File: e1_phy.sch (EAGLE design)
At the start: 125 parts, among them IC2 LD117AS33TR, IC3 LD117AS33TR, IC4 MCP4725, U1 IDT82V2081, U2 GPS_GNS_2201, U3 VCTCXO-CONNORWINFIELD, U4 VCXO_TAITIEN_VT, U5 IP4234CZ6, X2 SMA-142-0701-801/806, X3 JACK2.5_SJ-2523, X4 0446200002

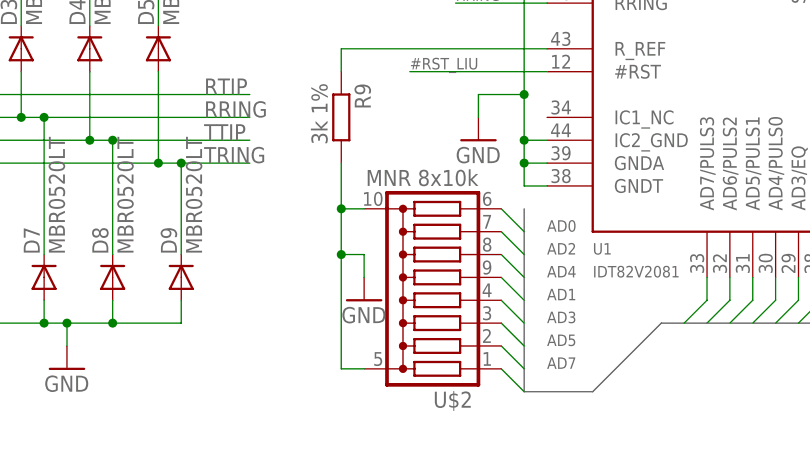
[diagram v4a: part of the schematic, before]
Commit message: Implementation of review comment:
   Removed octal resistor array, introduced quad resistor array,
   will be used for various pullups.
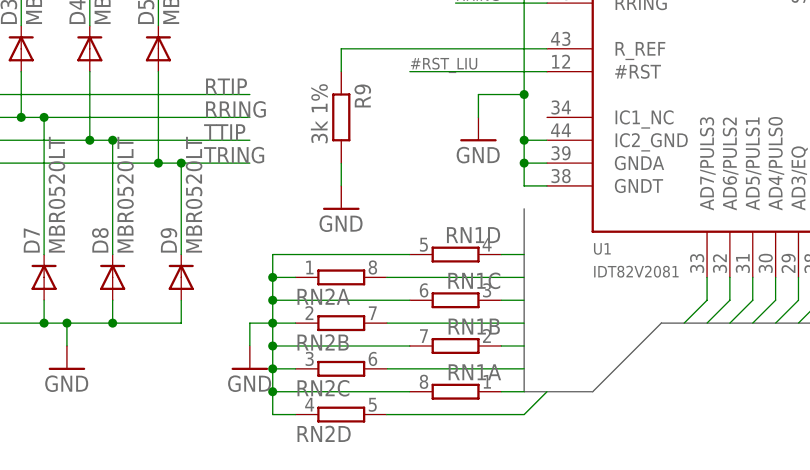
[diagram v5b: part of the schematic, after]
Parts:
- removed U$2: MNR 8x10k, laforge:MNR
- added RN1, RN2: (no value), resistor-dil:4R-NEXB38V
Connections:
- net AD0: now also RN2A.2; no longer U$2.8
- net AD1: now also RN2B.2; no longer U$2.4
- net AD2: now also RN2C.2; no longer U$2.7
- net AD3: now also RN2D.2; no longer U$2.3
- net AD4: now also RN1D.1; no longer U$2.6
- net AD5: now also RN1C.1; no longer U$2.2
- net AD6: now also RN1B.1; no longer U$2.5
- net AD7: now also RN1A.1; no longer U$2.1
- net GND: now also RN1A.2, RN1B.2, RN1C.2, RN1D.2, RN2A.1, RN2B.1, RN2C.1, RN2D.1; no longer U$2.C, U$2.D
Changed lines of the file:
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@@
 <part name="GND7" library="supply1" deviceset="GND" device=""/>
 <part name="GND8" library="supply1" deviceset="GND" device=""/>
-<part name="U$2" library="laforge" deviceset="MNR" device="" value="MNR 8x10k"/>
 <part name="GND9" library="supply1" deviceset="GND" device=""/>
 <part name="TR1" library="laforge" deviceset="PULSE_T1094NL" device=""/>
@@
 <part name="U5" library="laforge" deviceset="IP4234CZ6" device=""/>
 <part name="GND12" library="supply1" deviceset="GND" device=""/>
+<part name="RN1" library="resistor-dil" library_urn="urn:adsk.eagle:library:342" deviceset="4R-N" device="EXB38V" package3d_urn="urn:adsk.eagle:package:24923/1"/>
+<part name="RN2" library="resistor-dil" library_urn="urn:adsk.eagle:library:342" deviceset="4R-N" device="EXB38V" package3d_urn="urn:adsk.eagle:package:24923/1"/>
+<part name="GND28" library="supply1" deviceset="GND" device=""/>
 </parts>
 <sheets>
@@
 </instance>
 <instance part="GND8" gate="1" x="238.76" y="10.16"/>
-<instance part="U$2" gate="G$1" x="185.42" y="17.78" rot="R180"/>
-<instance part="GND9" gate="1" x="177.8" y="15.24"/>
+<instance part="GND9" gate="1" x="175.26" y="25.4"/>
 <instance part="TR1" gate="-1:1" x="93.98" y="40.64" rot="MR0"/>
 <instance part="TR1" gate="-1:2" x="93.98" y="17.78" rot="MR0"/>
@@
 <instance part="U5" gate="G$1" x="43.18" y="243.84"/>
 <instance part="GND12" gate="1" x="43.18" y="228.6"/>
+<instance part="RN1" gate="A" x="187.96" y="5.08" rot="R180"/>
+<instance part="RN1" gate="B" x="187.96" y="10.16" rot="R180"/>
+<instance part="RN1" gate="C" x="187.96" y="15.24" rot="R180"/>
+<instance part="RN1" gate="D" x="187.96" y="20.32" rot="R180"/>
+<instance part="RN2" gate="A" x="175.26" y="17.78"/>
+<instance part="RN2" gate="B" x="175.26" y="12.7"/>
+<instance part="RN2" gate="C" x="175.26" y="7.62"/>
+<instance part="RN2" gate="D" x="175.26" y="2.54"/>
+<instance part="GND28" gate="1" x="165.1" y="7.62"/>
 </instances>
 <busses>
@@
 </segment>
 <segment>
-<pinref part="U$2" gate="G$1" pin="C"/>
-<wire x1="177.8" y1="7.62" x2="175.26" y2="7.62" width="0.1524" layer="91"/>
 <pinref part="GND9" gate="1" pin="GND"/>
-<wire x1="175.26" y1="7.62" x2="175.26" y2="20.32" width="0.1524" layer="91"/>
-<pinref part="U$2" gate="G$1" pin="D"/>
-<wire x1="175.26" y1="20.32" x2="175.26" y2="25.4" width="0.1524" layer="91"/>
-<wire x1="175.26" y1="25.4" x2="177.8" y2="25.4" width="0.1524" layer="91"/>
-<wire x1="177.8" y1="17.78" x2="177.8" y2="20.32" width="0.1524" layer="91"/>
-<wire x1="177.8" y1="20.32" x2="175.26" y2="20.32" width="0.1524" layer="91"/>
-<junction x="175.26" y="20.32"/>
 <pinref part="R9" gate="G$1" pin="2"/>
-<wire x1="175.26" y1="30.48" x2="175.26" y2="25.4" width="0.1524" layer="91"/>
-<junction x="175.26" y="25.4"/>
+<wire x1="175.26" y1="30.48" x2="175.26" y2="27.94" width="0.1524" layer="91"/>
 </segment>
 <segment>
@@
 <pinref part="GND12" gate="1" pin="GND"/>
 <wire x1="43.18" y1="233.68" x2="43.18" y2="231.14" width="0.1524" layer="91"/>
+</segment>
+<segment>
+<pinref part="GND28" gate="1" pin="GND"/>
+<wire x1="165.1" y1="10.16" x2="165.1" y2="12.7" width="0.1524" layer="91"/>
+<pinref part="RN1" gate="D" pin="2"/>
+<wire x1="182.88" y1="20.32" x2="167.64" y2="20.32" width="0.1524" layer="91"/>
+<pinref part="RN2" gate="A" pin="1"/>
+<wire x1="170.18" y1="17.78" x2="167.64" y2="17.78" width="0.1524" layer="91"/>
+<wire x1="167.64" y1="17.78" x2="167.64" y2="20.32" width="0.1524" layer="91"/>
+<pinref part="RN1" gate="C" pin="2"/>
+<wire x1="182.88" y1="15.24" x2="167.64" y2="15.24" width="0.1524" layer="91"/>
+<wire x1="167.64" y1="15.24" x2="167.64" y2="17.78" width="0.1524" layer="91"/>
+<junction x="167.64" y="17.78"/>
+<pinref part="RN1" gate="B" pin="2"/>
+<wire x1="182.88" y1="10.16" x2="167.64" y2="10.16" width="0.1524" layer="91"/>
+<wire x1="167.64" y1="10.16" x2="167.64" y2="12.7" width="0.1524" layer="91"/>
+<junction x="167.64" y="15.24"/>
+<pinref part="RN2" gate="B" pin="1"/>
+<wire x1="167.64" y1="12.7" x2="167.64" y2="15.24" width="0.1524" layer="91"/>
+<wire x1="170.18" y1="12.7" x2="167.64" y2="12.7" width="0.1524" layer="91"/>
+<junction x="167.64" y="12.7"/>
+<pinref part="RN2" gate="C" pin="1"/>
+<wire x1="170.18" y1="7.62" x2="167.64" y2="7.62" width="0.1524" layer="91"/>
+<wire x1="167.64" y1="7.62" x2="167.64" y2="10.16" width="0.1524" layer="91"/>
+<junction x="167.64" y="10.16"/>
+<pinref part="RN2" gate="D" pin="1"/>
+<wire x1="170.18" y1="2.54" x2="167.64" y2="2.54" width="0.1524" layer="91"/>
+<wire x1="167.64" y1="2.54" x2="167.64" y2="5.08" width="0.1524" layer="91"/>
+<junction x="167.64" y="7.62"/>
+<pinref part="RN1" gate="A" pin="2"/>
+<wire x1="167.64" y1="5.08" x2="167.64" y2="7.62" width="0.1524" layer="91"/>
+<wire x1="182.88" y1="5.08" x2="167.64" y2="5.08" width="0.1524" layer="91"/>
+<junction x="167.64" y="5.08"/>
+<wire x1="165.1" y1="12.7" x2="167.64" y2="12.7" width="0.1524" layer="91"/>
 </segment>
 </net>
@@
 </segment>
 <segment>
-<pinref part="U$2" gate="G$1" pin="8"/>
-<wire x1="193.04" y1="25.4" x2="195.58" y2="22.86" width="0.1524" layer="91"/>
-<label x="198.12" y="22.86" size="1.27" layer="95"/>
+<pinref part="RN2" gate="A" pin="2"/>
+<wire x1="195.58" y1="17.78" x2="180.34" y2="17.78" width="0.1524" layer="91"/>
 </segment>
 </net>
@@
 </segment>
 <segment>
-<pinref part="U$2" gate="G$1" pin="4"/>
-<wire x1="193.04" y1="15.24" x2="195.58" y2="12.7" width="0.1524" layer="91"/>
-<label x="198.12" y="15.24" size="1.27" layer="95"/>
+<pinref part="RN2" gate="B" pin="2"/>
+<wire x1="195.58" y1="12.7" x2="180.34" y2="12.7" width="0.1524" layer="91"/>
 </segment>
 </net>
@@
 </segment>
 <segment>
-<pinref part="U$2" gate="G$1" pin="7"/>
-<wire x1="193.04" y1="22.86" x2="195.58" y2="20.32" width="0.1524" layer="91"/>
-<label x="198.12" y="20.32" size="1.27" layer="95"/>
+<pinref part="RN2" gate="C" pin="2"/>
+<wire x1="195.58" y1="7.62" x2="180.34" y2="7.62" width="0.1524" layer="91"/>
 </segment>
 </net>
@@
 </segment>
 <segment>
-<pinref part="U$2" gate="G$1" pin="3"/>
-<wire x1="193.04" y1="12.7" x2="195.58" y2="10.16" width="0.1524" layer="91"/>
-<label x="198.12" y="12.7" size="1.27" layer="95"/>
+<pinref part="RN2" gate="D" pin="2"/>
+<wire x1="180.34" y1="2.54" x2="195.58" y2="2.54" width="0.1524" layer="91"/>
+<wire x1="198.12" y1="5.08" x2="195.58" y2="2.54" width="0.1524" layer="91"/>
 </segment>
 </net>
@@
 </segment>
 <segment>
-<pinref part="U$2" gate="G$1" pin="6"/>
-<wire x1="193.04" y1="20.32" x2="195.58" y2="17.78" width="0.1524" layer="91"/>
-<label x="198.12" y="17.78" size="1.27" layer="95"/>
+<pinref part="RN1" gate="D" pin="1"/>
+<wire x1="193.04" y1="20.32" x2="195.58" y2="20.32" width="0.1524" layer="91"/>
 </segment>
 </net>
@@
 </segment>
 <segment>
-<pinref part="U$2" gate="G$1" pin="2"/>
-<wire x1="193.04" y1="10.16" x2="195.58" y2="7.62" width="0.1524" layer="91"/>
-<label x="198.12" y="10.16" size="1.27" layer="95"/>
+<pinref part="RN1" gate="C" pin="1"/>
+<wire x1="193.04" y1="15.24" x2="195.58" y2="15.24" width="0.1524" layer="91"/>
 </segment>
 </net>
@@
 </segment>
 <segment>
-<pinref part="U$2" gate="G$1" pin="5"/>
-<wire x1="193.04" y1="17.78" x2="195.58" y2="15.24" width="0.1524" layer="91"/>
+<pinref part="RN1" gate="B" pin="1"/>
+<wire x1="193.04" y1="10.16" x2="195.58" y2="10.16" width="0.1524" layer="91"/>
 </segment>
 </net>
@@
 </segment>
 <segment>
-<pinref part="U$2" gate="G$1" pin="1"/>
-<wire x1="193.04" y1="7.62" x2="195.58" y2="5.08" width="0.1524" layer="91"/>
-<label x="198.12" y="7.62" size="1.27" layer="95"/>
-</segment>
-</net>
+<pinref part="RN1" gate="A" pin="1"/>
+<wire x1="193.04" y1="5.08" x2="195.58" y2="5.08" width="0.1524" layer="91"/>
+</segment>
+</net>

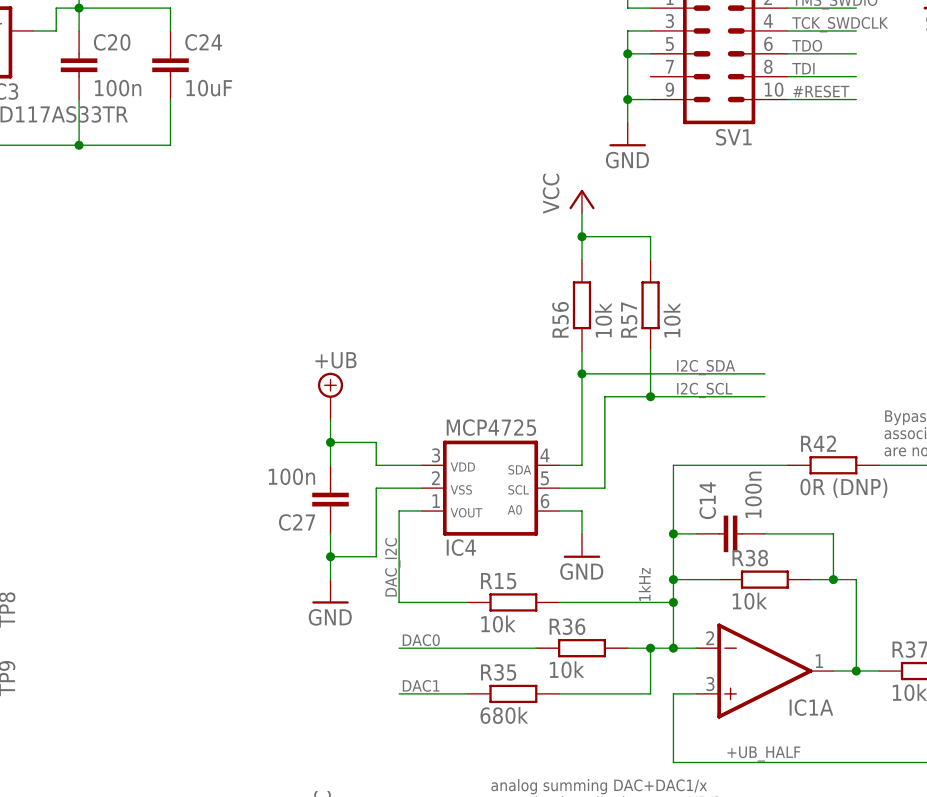
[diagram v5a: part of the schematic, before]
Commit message: Implement review comments: Switch DAC to Maxim part.
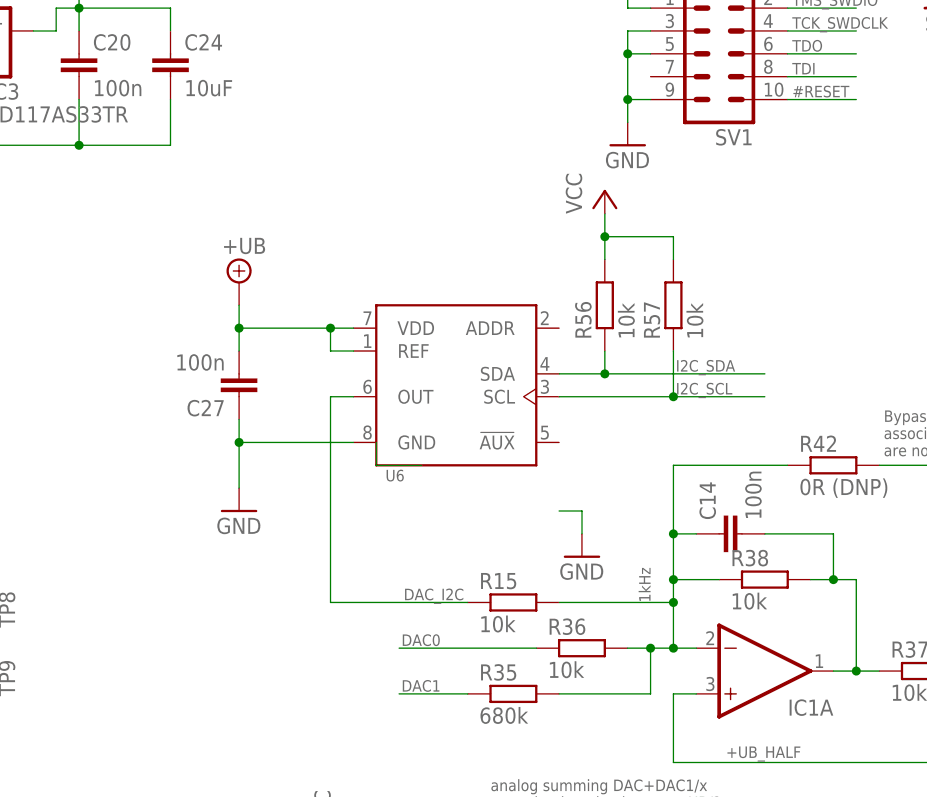
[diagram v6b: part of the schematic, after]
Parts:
- removed IC4: MCP4725, dp_devices:IC_MCP4725
- added U6: (no value), max5215_max5217:MAX521X
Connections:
- net +UB: now also U6.REF, U6.VDD; no longer IC4.3
- net DAC_I2C: now also U6.OUT; no longer IC4.1
- net GND: now also U6.GND; no longer IC4.2, IC4.6
- net I2C_SCL: now also U6.SCL; no longer IC4.5
- net I2C_SDA: now also U6.SDA; no longer IC4.4
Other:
- moved on the sheet: C27, R56, R57
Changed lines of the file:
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@@
 <part name="TP14" library="testpad" deviceset="TP" device="B1,27"/>
 <part name="TP15" library="testpad" deviceset="TP" device="B1,27"/>
-<part name="IC4" library="dp_devices" deviceset="IC_MCP4725" device="" value="MCP4725"/>
 <part name="C27" library="rcl" deviceset="C-EU" device="C0603" value="100n"/>
 <part name="SUPPLY7" library="supply2" deviceset="+UB" device=""/>
@@
 <part name="RN2" library="resistor-dil" library_urn="urn:adsk.eagle:library:342" deviceset="4R-N" device="EXB38V" package3d_urn="urn:adsk.eagle:package:24923/1"/>
 <part name="GND28" library="supply1" deviceset="GND" device=""/>
+<part name="U6" library="max5215_max5217" deviceset="MAX521X" device=""/>
 </parts>
 <sheets>
@@
 <instance part="TP14" gate="G$1" x="109.22" y="106.68" rot="R180"/>
 <instance part="TP15" gate="G$1" x="111.76" y="104.14" rot="R180"/>
-<instance part="IC4" gate="G$1" x="233.68" y="195.58" rot="MR180"/>
-<instance part="C27" gate="G$1" x="215.9" y="193.04" rot="R180"/>
-<instance part="SUPPLY7" gate="G$1" x="215.9" y="205.74"/>
-<instance part="GND34" gate="1" x="215.9" y="182.88"/>
+<instance part="C27" gate="G$1" x="205.74" y="205.74" rot="R180"/>
+<instance part="SUPPLY7" gate="G$1" x="205.74" y="218.44"/>
+<instance part="GND34" gate="1" x="205.74" y="193.04"/>
 <instance part="R15" gate="G$1" x="236.22" y="182.88"/>
 <instance part="GND35" gate="1" x="243.84" y="187.96"/>
@@
 </instance>
 <instance part="GND30" gate="G$1" x="20.32" y="48.26"/>
-<instance part="R56" gate="G$1" x="243.84" y="215.9" rot="R90"/>
-<instance part="R57" gate="G$1" x="251.46" y="215.9" rot="R90"/>
-<instance part="P+4" gate="VCC" x="243.84" y="228.6"/>
+<instance part="R56" gate="G$1" x="246.38" y="215.9" rot="R90"/>
+<instance part="R57" gate="G$1" x="254" y="215.9" rot="R90"/>
+<instance part="P+4" gate="VCC" x="246.38" y="228.6"/>
 <instance part="JP2" gate="A" x="144.78" y="210.82" rot="R270"/>
 <instance part="U1" gate="G$1" x="226.06" y="45.72"/>
@@
 <instance part="RN2" gate="D" x="175.26" y="2.54"/>
 <instance part="GND28" gate="1" x="165.1" y="7.62"/>
+<instance part="U6" gate="G$1" x="228.6" y="205.74"/>
 </instances>
 <busses>
@@
 </segment>
 <segment>
+<pinref part="GND34" gate="1" pin="GND"/>
 <pinref part="C27" gate="G$1" pin="1"/>
-<pinref part="GND34" gate="1" pin="GND"/>
-<wire x1="215.9" y1="190.5" x2="215.9" y2="187.96" width="0.1524" layer="91"/>
-<pinref part="IC4" gate="G$1" pin="2"/>
-<wire x1="215.9" y1="187.96" x2="215.9" y2="185.42" width="0.1524" layer="91"/>
-<wire x1="226.06" y1="195.58" x2="220.98" y2="195.58" width="0.1524" layer="91"/>
-<wire x1="220.98" y1="195.58" x2="220.98" y2="187.96" width="0.1524" layer="91"/>
-<wire x1="220.98" y1="187.96" x2="215.9" y2="187.96" width="0.1524" layer="91"/>
-<junction x="215.9" y="187.96"/>
-</segment>
-<segment>
-<pinref part="IC4" gate="G$1" pin="6"/>
+<wire x1="205.74" y1="203.2" x2="205.74" y2="200.66" width="0.1524" layer="91"/>
+<pinref part="U6" gate="G$1" pin="GND"/>
+<wire x1="205.74" y1="200.66" x2="205.74" y2="195.58" width="0.1524" layer="91"/>
+<wire x1="218.44" y1="200.66" x2="205.74" y2="200.66" width="0.1524" layer="91"/>
+<junction x="205.74" y="200.66"/>
+</segment>
+<segment>
 <wire x1="241.3" y1="193.04" x2="243.84" y2="193.04" width="0.1524" layer="91"/>
 <wire x1="243.84" y1="193.04" x2="243.84" y2="190.5" width="0.1524" layer="91"/>
@@
 <pinref part="P+4" gate="VCC" pin="VCC"/>
 <pinref part="R56" gate="G$1" pin="2"/>
-<wire x1="243.84" y1="226.06" x2="243.84" y2="223.52" width="0.1524" layer="91"/>
-<wire x1="243.84" y1="223.52" x2="243.84" y2="220.98" width="0.1524" layer="91"/>
-<wire x1="243.84" y1="223.52" x2="251.46" y2="223.52" width="0.1524" layer="91"/>
-<junction x="243.84" y="223.52"/>
+<wire x1="246.38" y1="226.06" x2="246.38" y2="223.52" width="0.1524" layer="91"/>
+<wire x1="246.38" y1="223.52" x2="246.38" y2="220.98" width="0.1524" layer="91"/>
+<wire x1="246.38" y1="223.52" x2="254" y2="223.52" width="0.1524" layer="91"/>
+<junction x="246.38" y="223.52"/>
 <pinref part="R57" gate="G$1" pin="2"/>
-<wire x1="251.46" y1="223.52" x2="251.46" y2="220.98" width="0.1524" layer="91"/>
+<wire x1="254" y1="223.52" x2="254" y2="220.98" width="0.1524" layer="91"/>
 </segment>
 <segment>
@@
 </segment>
 <segment>
+<pinref part="C27" gate="G$1" pin="2"/>
 <pinref part="SUPPLY7" gate="G$1" pin="+UB"/>
-<pinref part="C27" gate="G$1" pin="2"/>
-<wire x1="215.9" y1="203.2" x2="215.9" y2="200.66" width="0.1524" layer="91"/>
-<pinref part="IC4" gate="G$1" pin="3"/>
-<wire x1="215.9" y1="200.66" x2="215.9" y2="198.12" width="0.1524" layer="91"/>
-<wire x1="226.06" y1="198.12" x2="220.98" y2="198.12" width="0.1524" layer="91"/>
-<wire x1="220.98" y1="198.12" x2="220.98" y2="200.66" width="0.1524" layer="91"/>
-<wire x1="220.98" y1="200.66" x2="215.9" y2="200.66" width="0.1524" layer="91"/>
-<junction x="215.9" y="200.66"/>
+<wire x1="205.74" y1="215.9" x2="205.74" y2="213.36" width="0.1524" layer="91"/>
+<pinref part="U6" gate="G$1" pin="VDD"/>
+<wire x1="205.74" y1="213.36" x2="205.74" y2="210.82" width="0.1524" layer="91"/>
+<wire x1="218.44" y1="213.36" x2="215.9" y2="213.36" width="0.1524" layer="91"/>
+<junction x="205.74" y="213.36"/>
+<pinref part="U6" gate="G$1" pin="REF"/>
+<wire x1="215.9" y1="213.36" x2="205.74" y2="213.36" width="0.1524" layer="91"/>
+<wire x1="218.44" y1="210.82" x2="215.9" y2="210.82" width="0.1524" layer="91"/>
+<wire x1="215.9" y1="210.82" x2="215.9" y2="213.36" width="0.1524" layer="91"/>
+<junction x="215.9" y="213.36"/>
 </segment>
 <segment>
@@
 </segment>
 <segment>
-<pinref part="IC4" gate="G$1" pin="4"/>
-<wire x1="241.3" y1="198.12" x2="243.84" y2="198.12" width="0.1524" layer="91"/>
-<wire x1="243.84" y1="198.12" x2="243.84" y2="208.28" width="0.1524" layer="91"/>
+<wire x1="241.3" y1="208.28" x2="246.38" y2="208.28" width="0.1524" layer="91"/>
 <label x="254.254" y="208.534" size="1.27" layer="95"/>
-<wire x1="243.84" y1="208.28" x2="264.16" y2="208.28" width="0.1524" layer="91"/>
+<wire x1="246.38" y1="208.28" x2="264.16" y2="208.28" width="0.1524" layer="91"/>
 <pinref part="R56" gate="G$1" pin="1"/>
-<wire x1="243.84" y1="210.82" x2="243.84" y2="208.28" width="0.1524" layer="91"/>
-<junction x="243.84" y="208.28"/>
+<wire x1="246.38" y1="210.82" x2="246.38" y2="208.28" width="0.1524" layer="91"/>
+<junction x="246.38" y="208.28"/>
+<pinref part="U6" gate="G$1" pin="SDA"/>
 </segment>
 </net>
@@
 </segment>
 <segment>
-<pinref part="IC4" gate="G$1" pin="5"/>
-<wire x1="241.3" y1="195.58" x2="246.38" y2="195.58" width="0.1524" layer="91"/>
-<wire x1="246.38" y1="195.58" x2="246.38" y2="205.74" width="0.1524" layer="91"/>
 <label x="254.254" y="205.994" size="1.27" layer="95"/>
-<wire x1="246.38" y1="205.74" x2="251.46" y2="205.74" width="0.1524" layer="91"/>
+<wire x1="241.3" y1="205.74" x2="254" y2="205.74" width="0.1524" layer="91"/>
 <pinref part="R57" gate="G$1" pin="1"/>
-<wire x1="251.46" y1="205.74" x2="264.16" y2="205.74" width="0.1524" layer="91"/>
-<wire x1="251.46" y1="210.82" x2="251.46" y2="205.74" width="0.1524" layer="91"/>
-<junction x="251.46" y="205.74"/>
+<wire x1="254" y1="205.74" x2="264.16" y2="205.74" width="0.1524" layer="91"/>
+<wire x1="254" y1="210.82" x2="254" y2="205.74" width="0.1524" layer="91"/>
+<junction x="254" y="205.74"/>
+<pinref part="U6" gate="G$1" pin="SCL"/>
 </segment>
 </net>
@@
 <segment>
 <pinref part="R15" gate="G$1" pin="1"/>
-<wire x1="231.14" y1="182.88" x2="223.52" y2="182.88" width="0.1524" layer="91"/>
-<wire x1="223.52" y1="182.88" x2="223.52" y2="193.04" width="0.1524" layer="91"/>
-<pinref part="IC4" gate="G$1" pin="1"/>
-<wire x1="223.52" y1="193.04" x2="226.06" y2="193.04" width="0.1524" layer="91"/>
-<label x="223.266" y="183.388" size="1.27" layer="95" rot="R90"/>
+<label x="224.028" y="183.134" size="1.27" layer="95"/>
+<pinref part="U6" gate="G$1" pin="OUT"/>
+<wire x1="218.44" y1="205.74" x2="215.9" y2="205.74" width="0.1524" layer="91"/>
+<wire x1="215.9" y1="205.74" x2="215.9" y2="182.88" width="0.1524" layer="91"/>
+<wire x1="215.9" y1="182.88" x2="231.14" y2="182.88" width="0.1524" layer="91"/>
 </segment>
 </net>
@@
 </segment>
 </net>
+<net name="N$12" class="0">
+<segment>
+<wire x1="226.06" y1="198.12" x2="220.98" y2="198.12" width="0.1524" layer="91"/>
+<wire x1="220.98" y1="198.12" x2="220.98" y2="200.66" width="0.1524" layer="91"/>
+</segment>
+</net>
